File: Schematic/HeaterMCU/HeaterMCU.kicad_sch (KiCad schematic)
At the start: 57 parts, among them J301 To PSU Board, J302 To µTracer, J303 Firmware, Q301 BSS138, Q302 BSS138, SW301 RESET, U301 INA219AIDCNR, U302 Display_IPS_1.3_SPI, U303 ATMEGA328P-AU, U304 TPS54302, Y301 8MHz

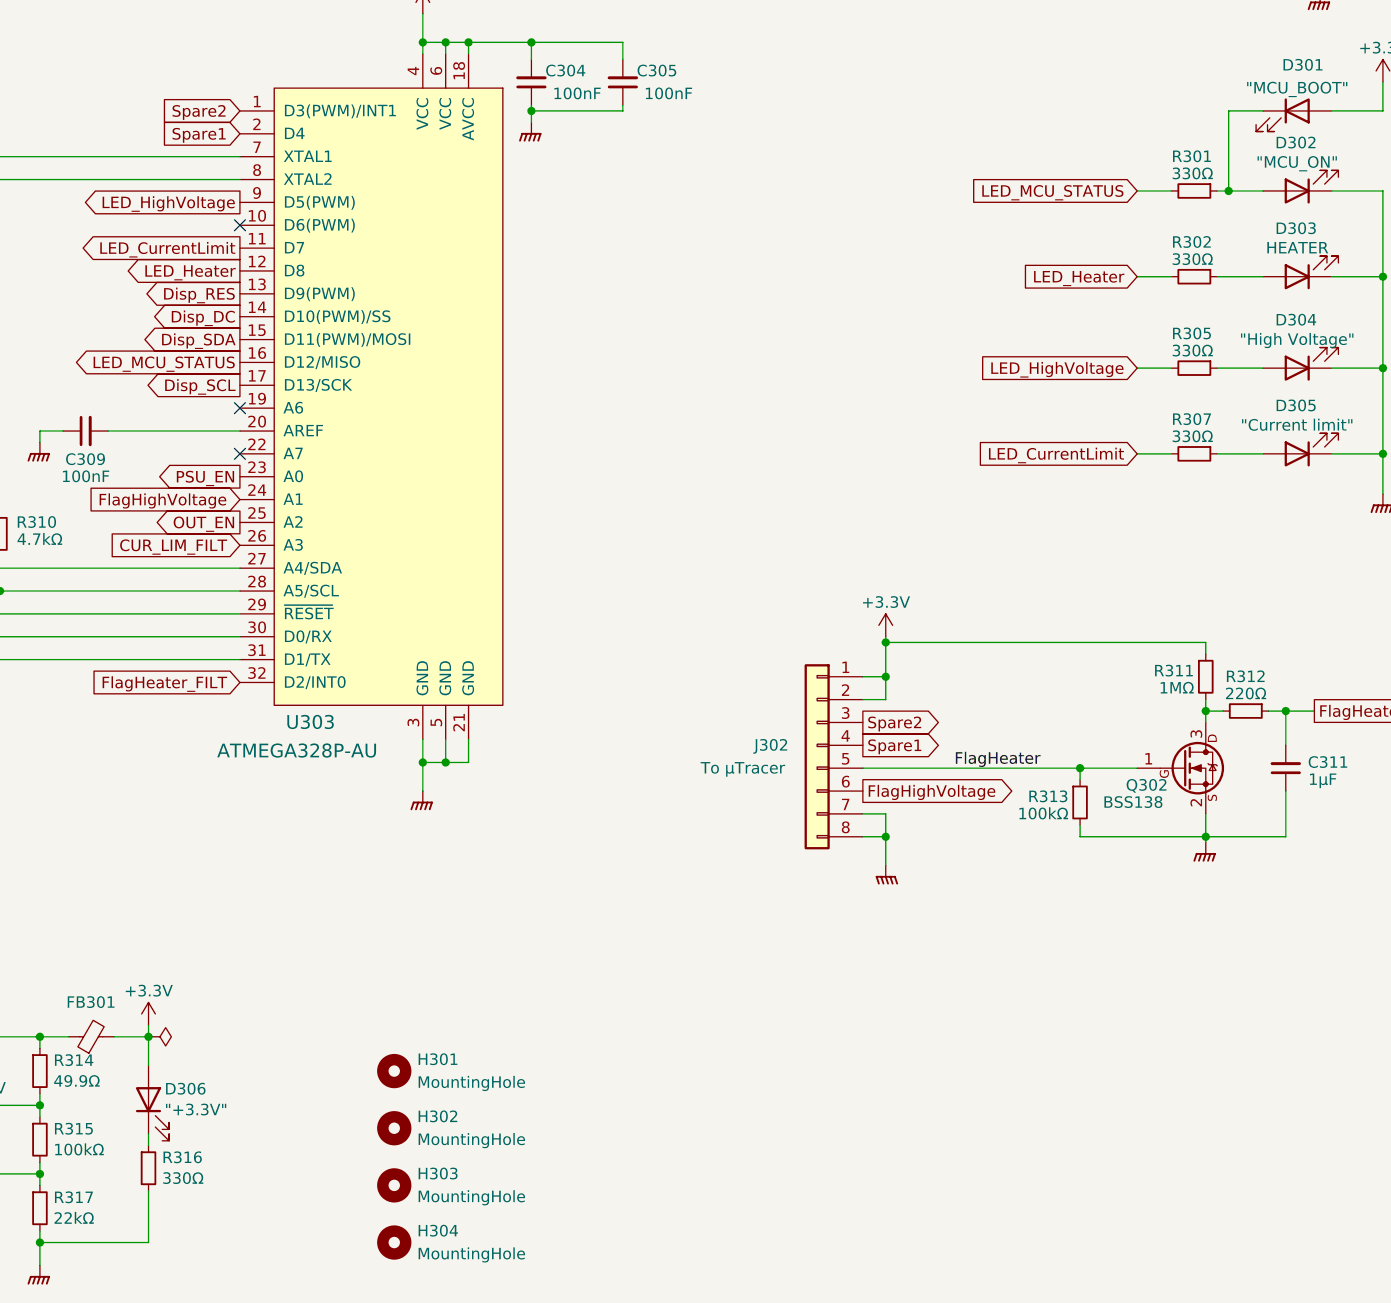
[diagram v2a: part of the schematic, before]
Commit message: Updated component values
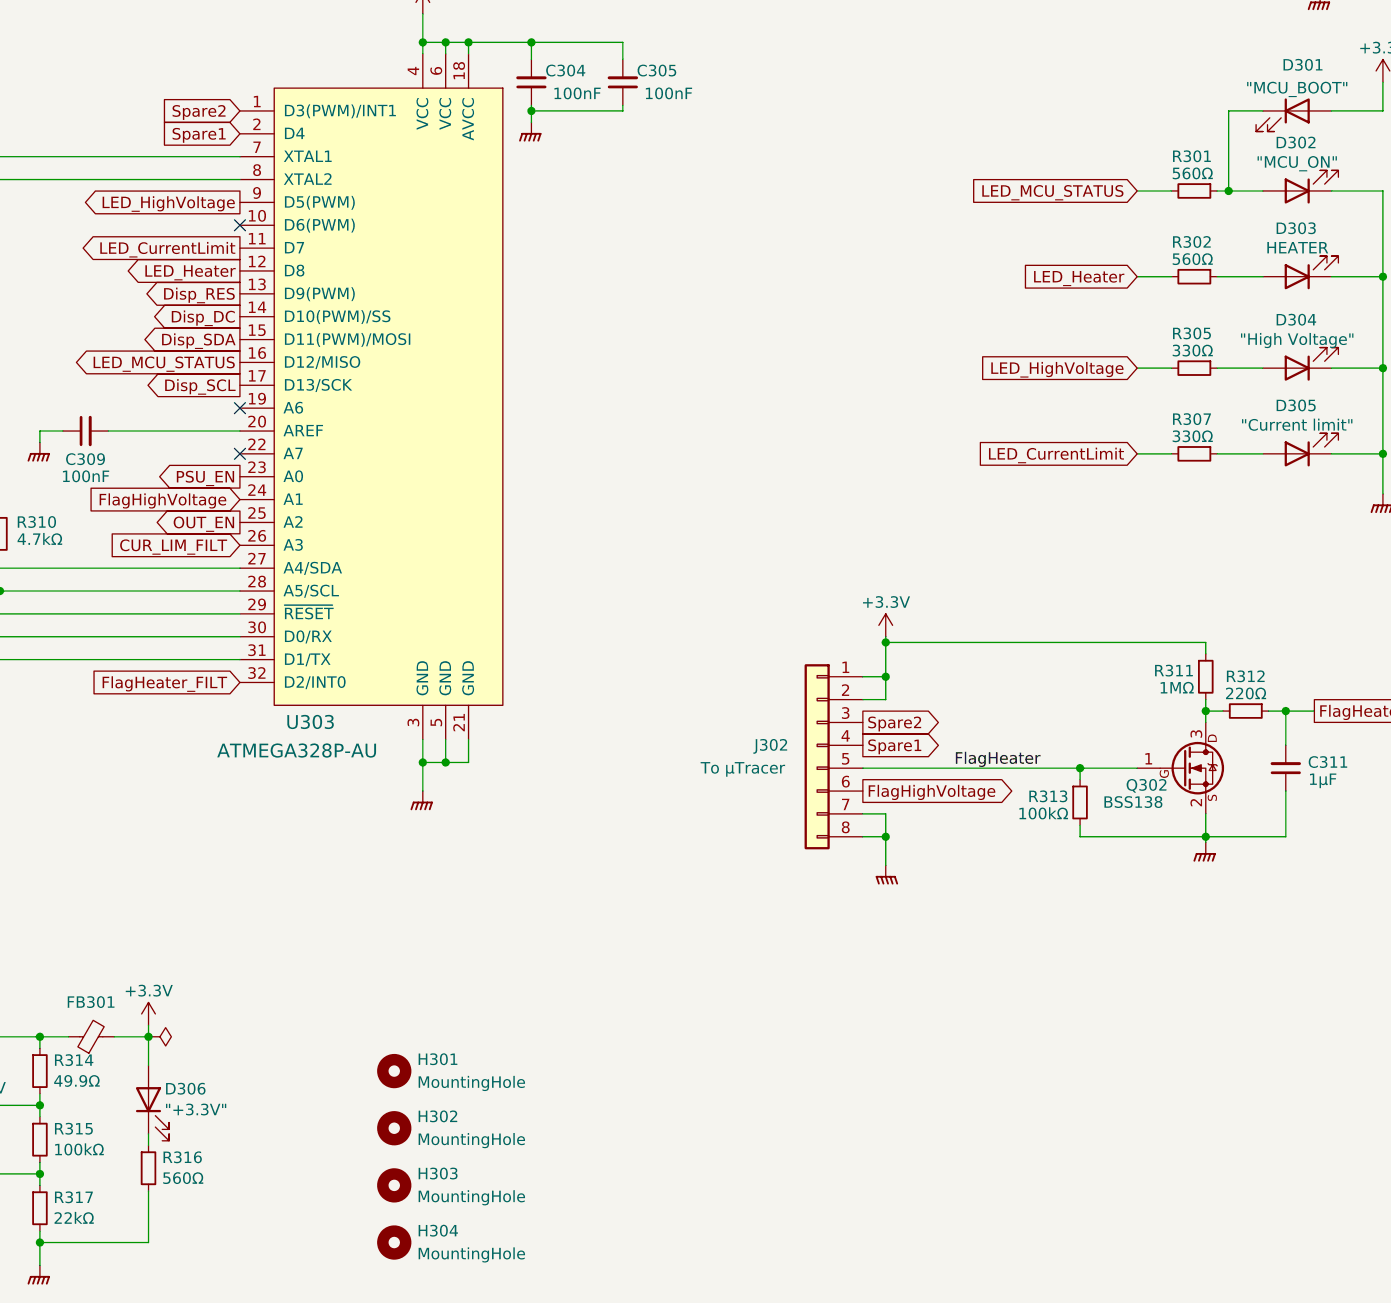
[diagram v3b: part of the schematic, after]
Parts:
- R301, R302, R316: value 330Ω -> 560Ω
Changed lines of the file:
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@@
       (effects (font (size 1.27 1.27)) (justify left))
     )
-    (property "Value" "330Ω" (id 1) (at 237.49 74.295 90)
+    (property "Value" "560Ω" (id 1) (at 237.49 74.295 90)
       (effects (font (size 1.27 1.27)) (justify left))
     )
@@
       (effects (font (size 1.27 1.27)) (justify left))
     )
-    (property "Value" "330Ω" (id 1) (at 125.3236 176.403 0)
+    (property "Value" "560Ω" (id 1) (at 125.3236 176.403 0)
       (effects (font (size 1.27 1.27)) (justify left))
     )
@@
       (effects (font (size 1.27 1.27)) (justify left))
     )
-    (property "Value" "330Ω" (id 1) (at 237.49 64.77 90)
+    (property "Value" "560Ω" (id 1) (at 237.49 64.77 90)
       (effects (font (size 1.27 1.27)) (justify left))
     )
@@
     )
     (path "/70e921c9-9afe-4b38-afa0-ace94eae71a3"
-      (reference "R301") (unit 1) (value "330Ω") (footprint "Resistor_SMD:R_0603_1608Metric_Pad0.98x0.95mm_HandSolder")
+      (reference "R301") (unit 1) (value "560Ω") (footprint "Resistor_SMD:R_0603_1608Metric_Pad0.98x0.95mm_HandSolder")
     )
     (path "/183290ea-f29b-4259-ab3f-5f72f5a8e50e"
-      (reference "R302") (unit 1) (value "330Ω") (footprint "Resistor_SMD:R_0603_1608Metric_Pad0.98x0.95mm_HandSolder")
+      (reference "R302") (unit 1) (value "560Ω") (footprint "Resistor_SMD:R_0603_1608Metric_Pad0.98x0.95mm_HandSolder")
     )
     (path "/ff36cb46-f6c9-438f-bf37-f9dd515118e3"
@@
     )
     (path "/50a185bc-674e-4c14-bfd7-3e020239554a"
-      (reference "R316") (unit 1) (value "330Ω") (footprint "Resistor_SMD:R_0603_1608Metric_Pad0.98x0.95mm_HandSolder")
+      (reference "R316") (unit 1) (value "560Ω") (footprint "Resistor_SMD:R_0603_1608Metric_Pad0.98x0.95mm_HandSolder")
     )
     (path "/6427c9b7-89c8-4be9-863c-fb53d3585861"

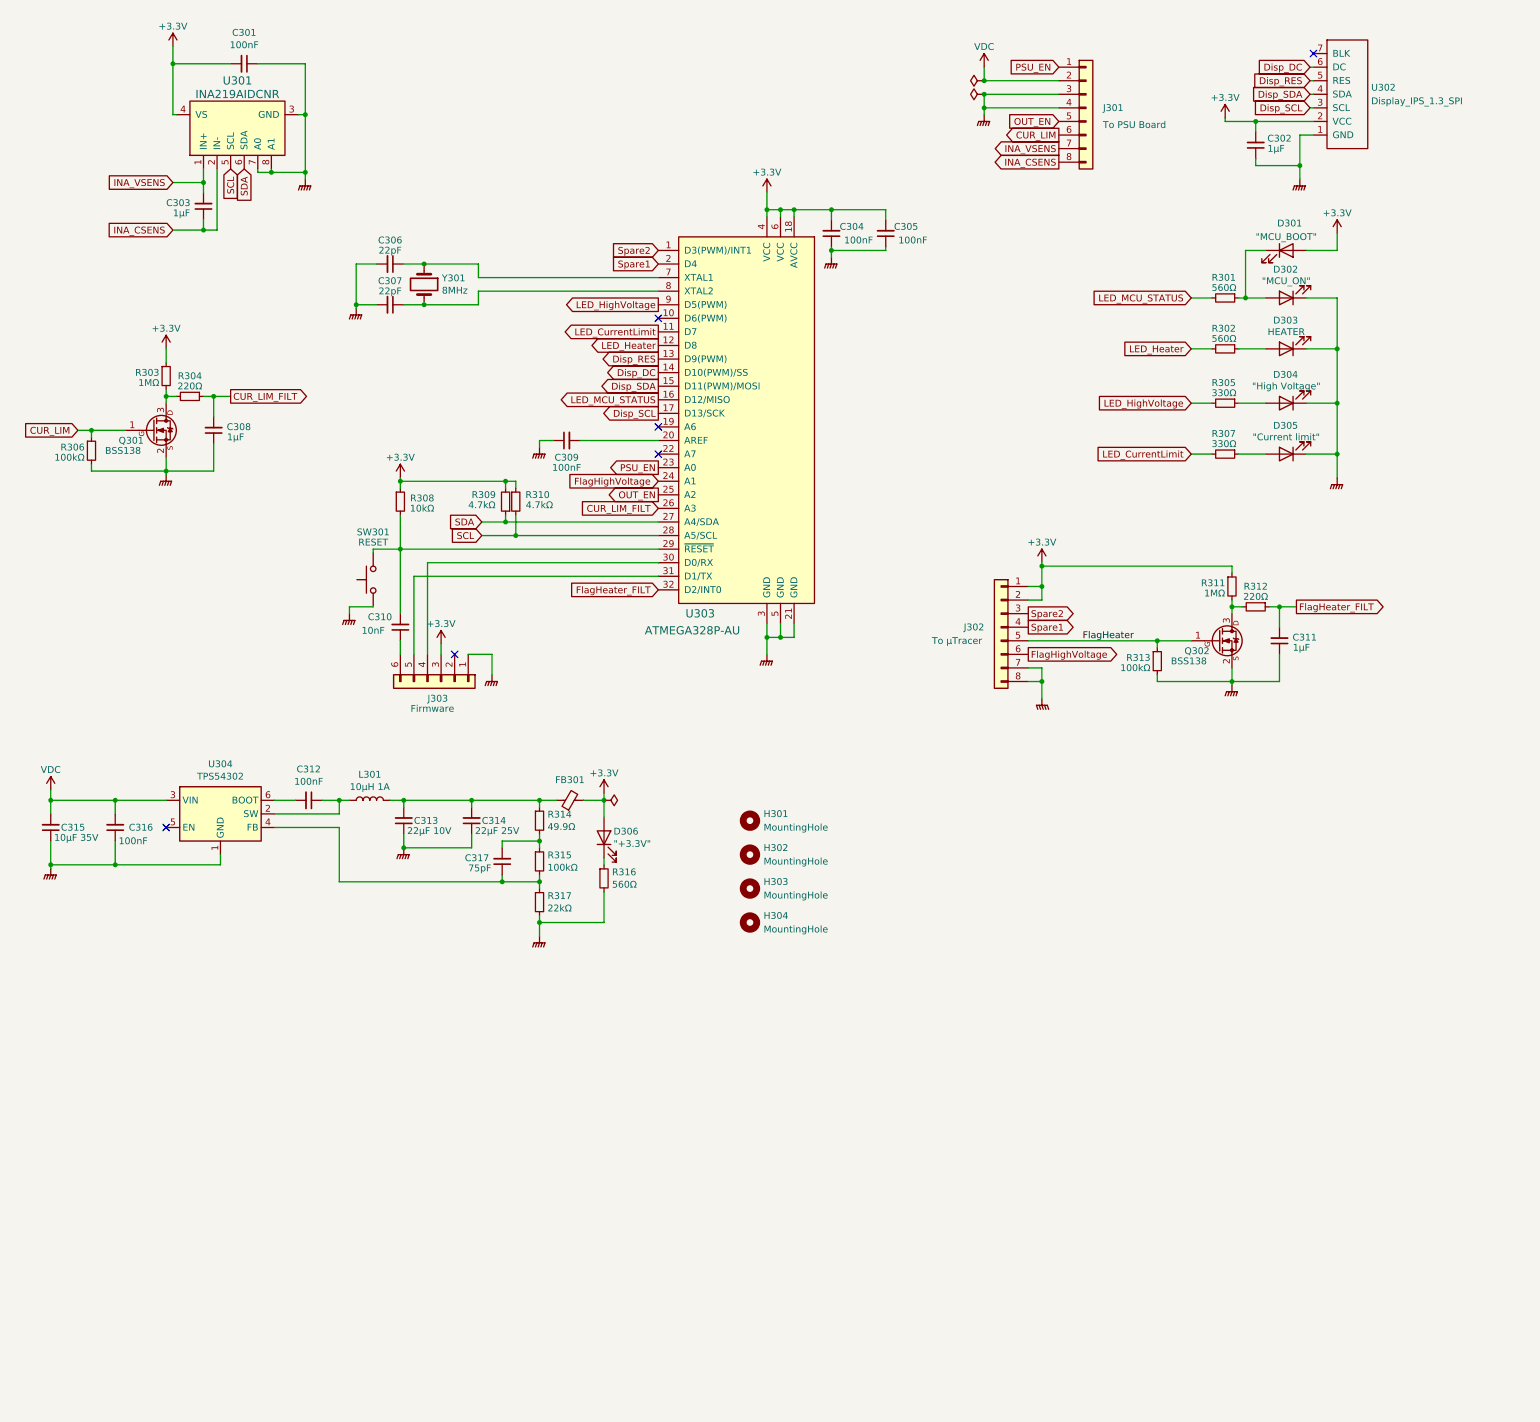
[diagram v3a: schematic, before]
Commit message: Rearranged schematic
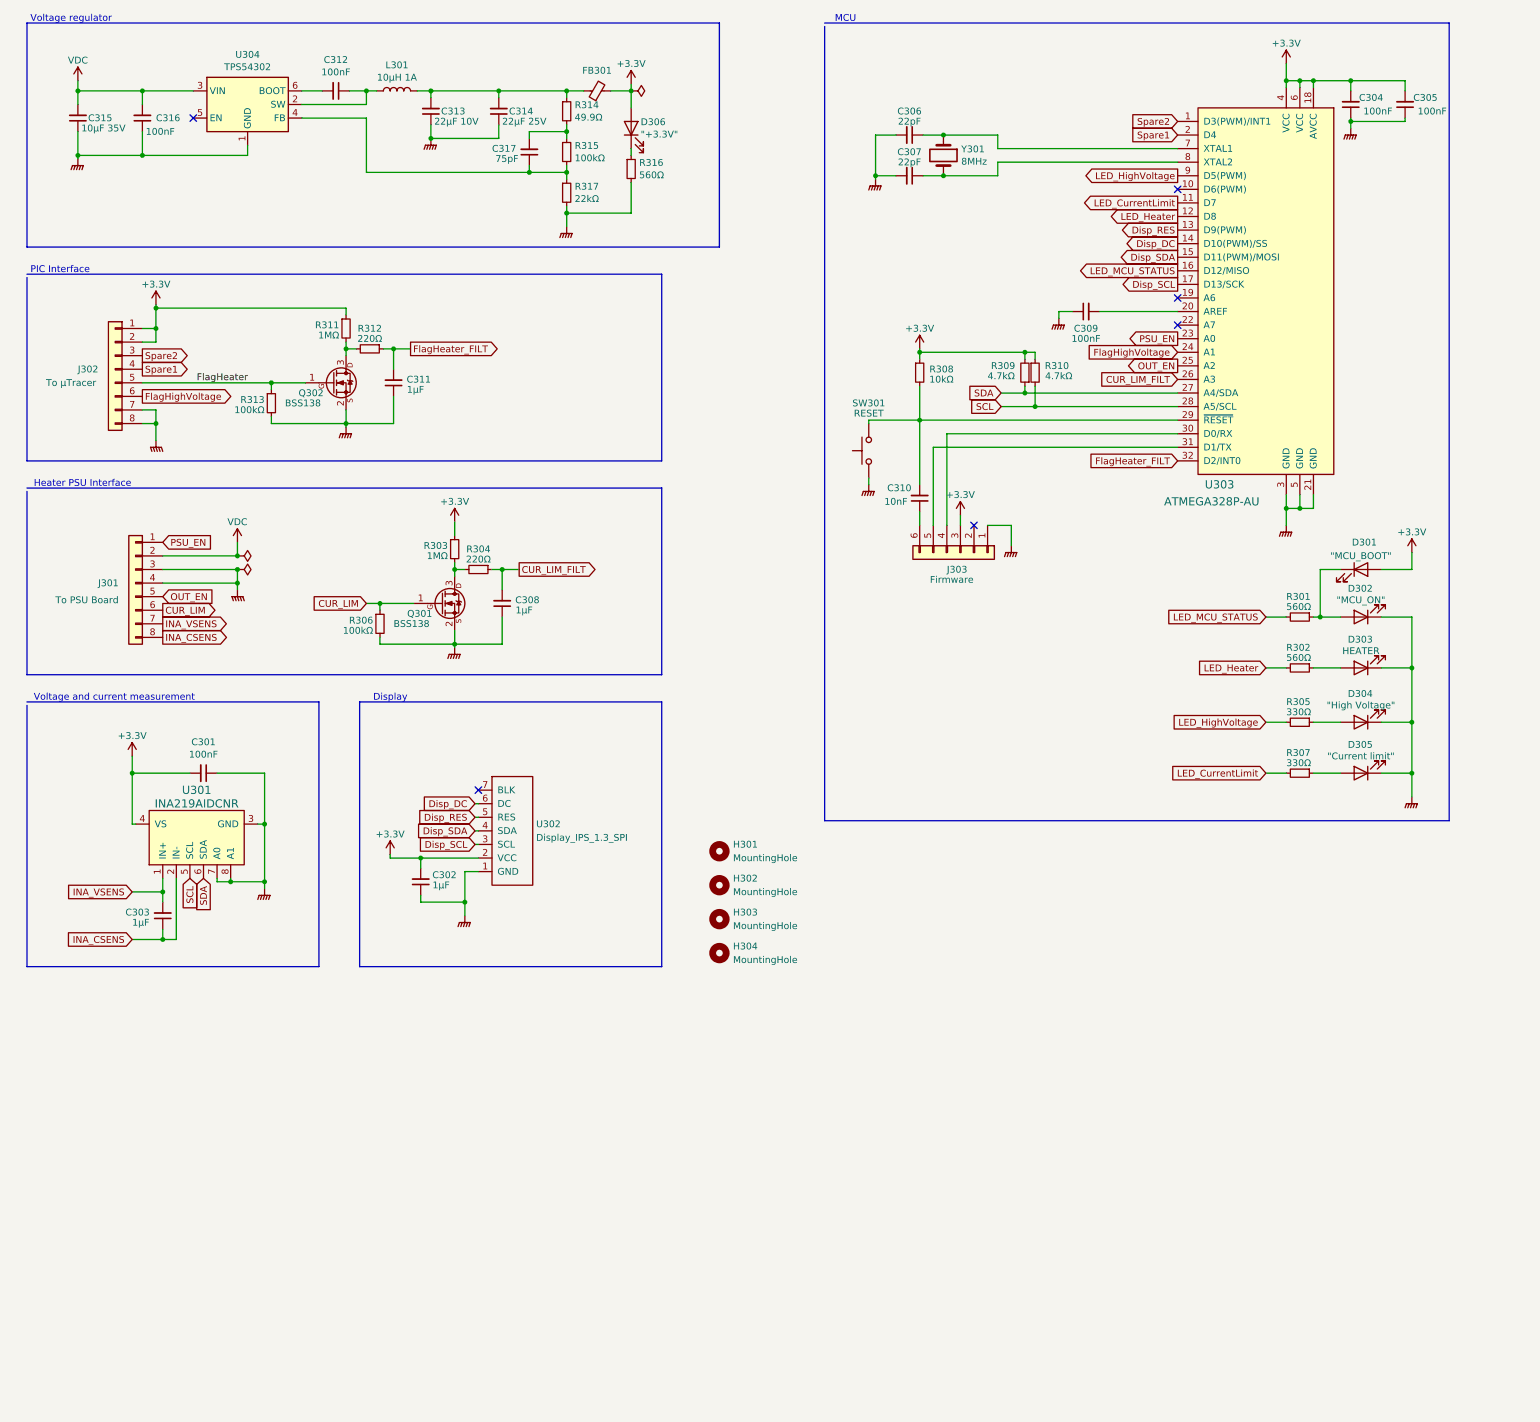
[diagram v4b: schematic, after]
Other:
- note added: "Display"
- note added: "Heater PSU Interface"
- note added: "MCU"
- note added: "PIC Interface"
- note added: "Voltage and current measurement"
- note added: "Voltage regulator"
- company: (none) -> Retronics - Bjørner Sandom
- title: (none) -> uTracer Heater - MCU Board
- moved on the sheet: C301, C302, C303, C304, C305, C306, C307, C308, C309, C310, C311, C312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
